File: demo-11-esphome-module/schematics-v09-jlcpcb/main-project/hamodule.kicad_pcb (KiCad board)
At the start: 2 copper layers, 145.4 x 76.2 mm, 64 parts, among them J1 1017505, J2 Conn-ESP-Relays, J3 1017505, J4 Conn-Buttons, J5 Conn_01x02, J6 Conn-Esp-Sensors, J7 Conn-LedIndicators, J8 1017505, J9 Current Jumper, K1 G5Q-1, K2 G5Q-1, K3 G5Q-1, K4 G5Q-1, U1 ULN2003A, U2 LD1117S33TR_SOT223, U3 HCPL3700, U4 HCPL3700, U5 HCPL3700, U6 HCPL3700

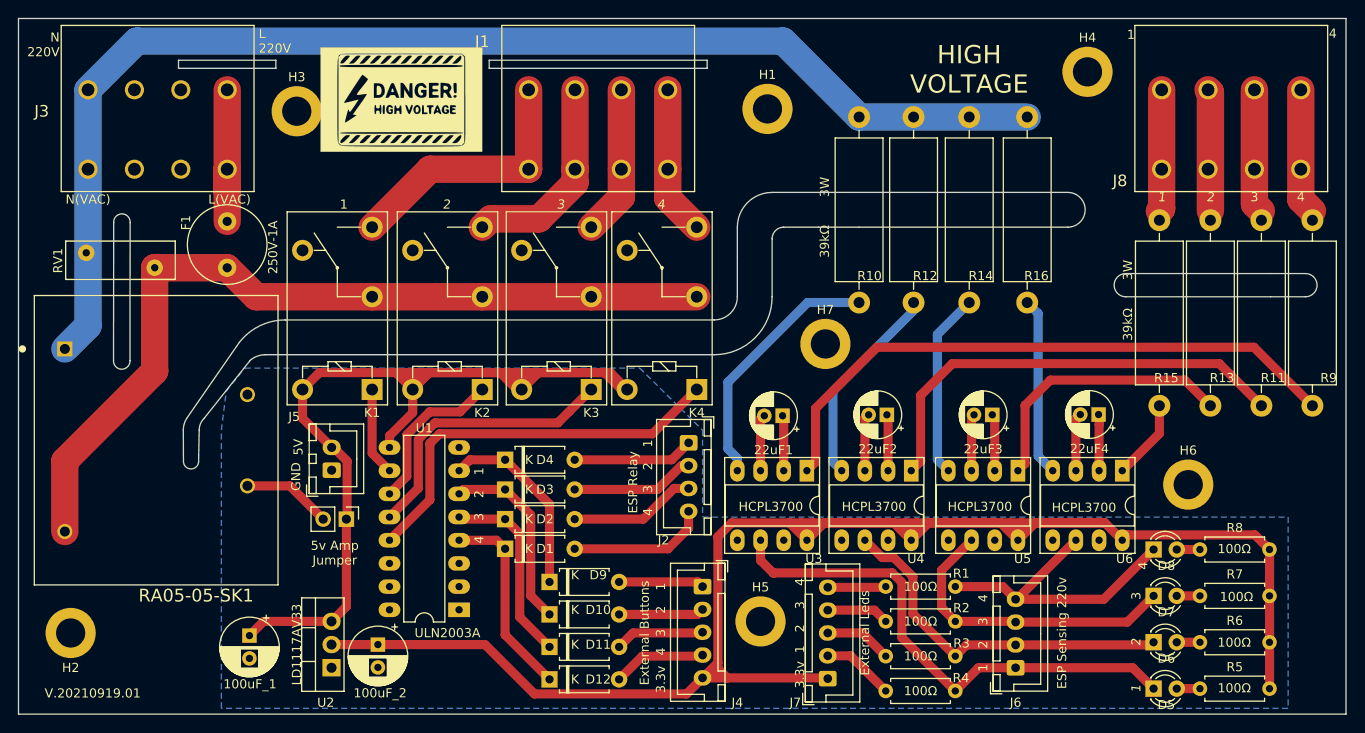
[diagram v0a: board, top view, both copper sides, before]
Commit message: jlcpcb v2: increas connectors pads + fix numbering for sensors in labels
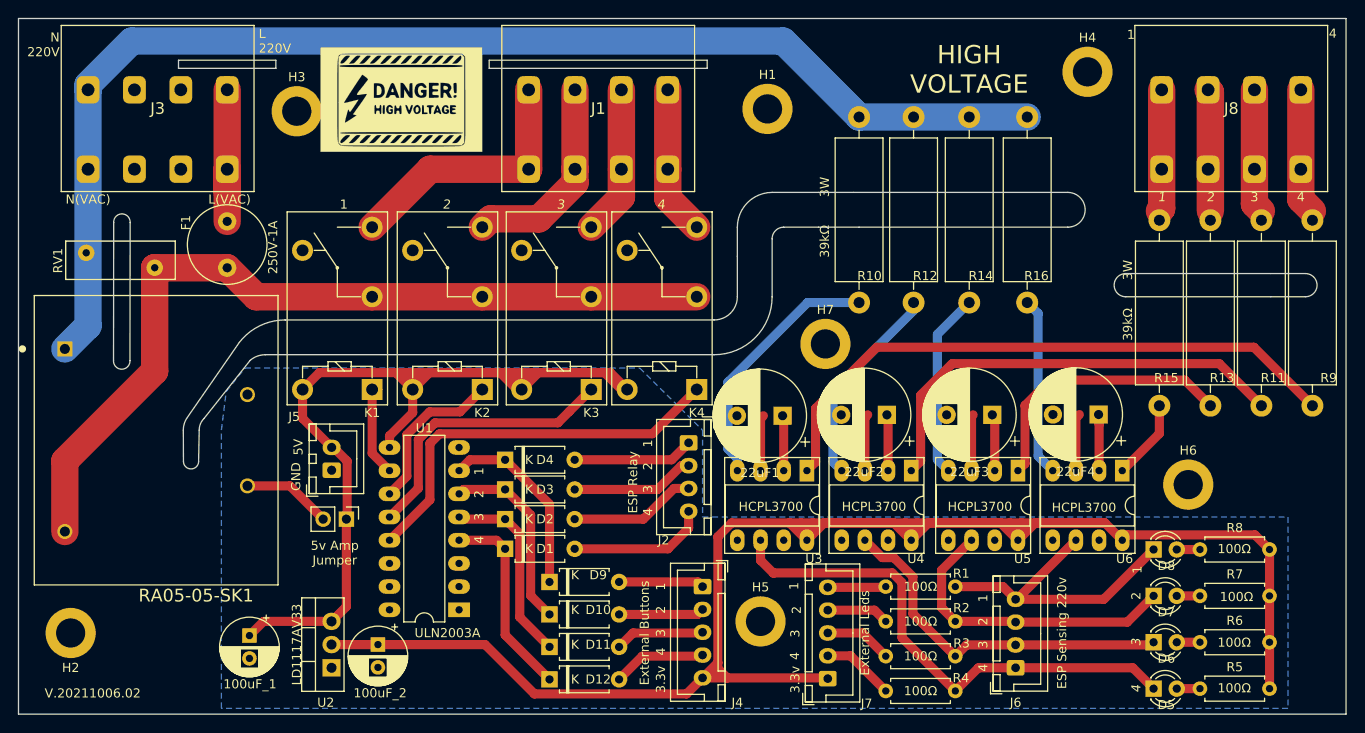
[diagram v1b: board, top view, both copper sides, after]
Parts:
- 22uF1, 22uF2, 22uF3, 22uF4: footprint Capacitor_THT:CP_Radial_D5.0mm_P2.00mm -> Capacitor_THT:CP_Radial_D10.0mm_P5.00mm
- J1, J3, J8: footprint Phoenix_Conn:1017505 -> 1017505_updated_pretty:1017505_pretty
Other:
- board text added: "V.20211006.02"
- board text removed: "V.20210919.01"

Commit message: adding an output fuse
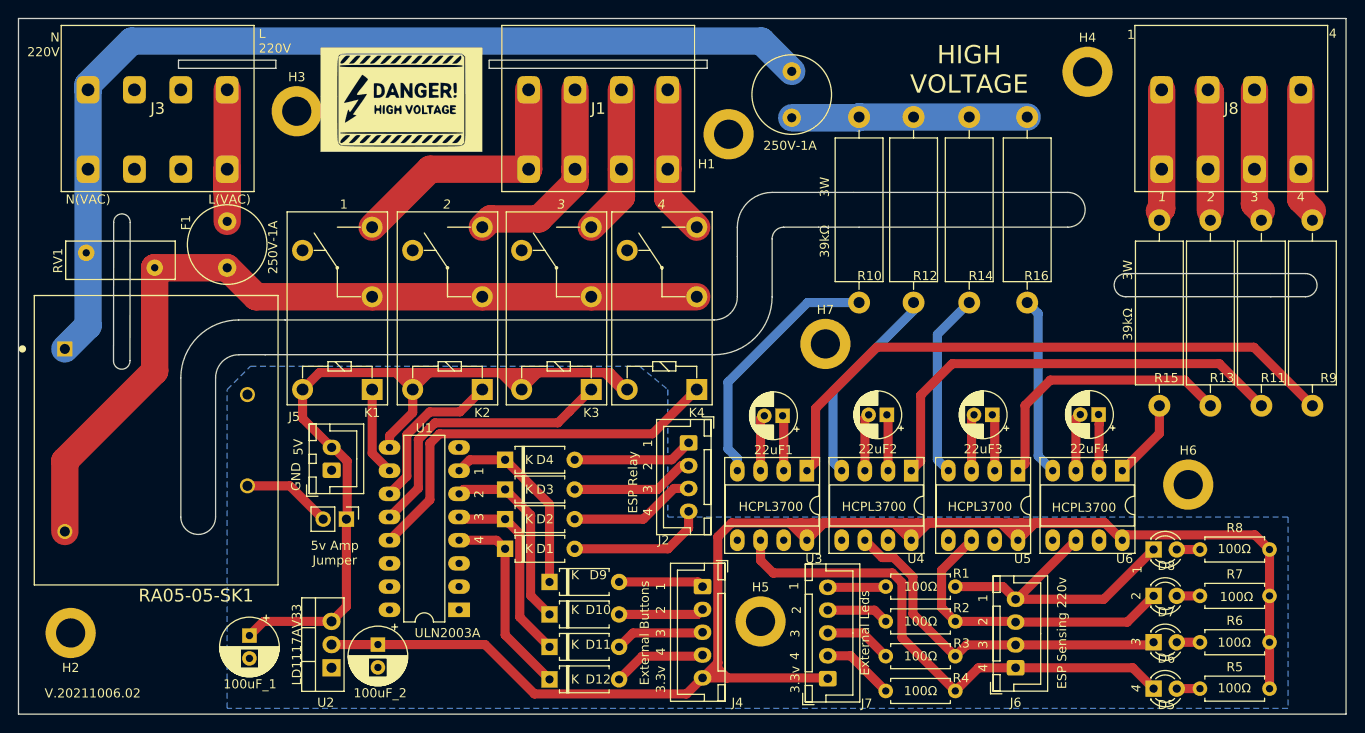
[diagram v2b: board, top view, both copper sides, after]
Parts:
- added 250V-1A: F250V, Fuse:Fuse_Littelfuse_372_D8.50mm, F.Cu at (106.3, 17.2)
- 22uF1, 22uF2, 22uF3, 22uF4: footprint Capacitor_THT:CP_Radial_D10.0mm_P5.00mm -> Capacitor_THT:CP_Radial_D5.0mm_P2.00mm
- F1: value Fuse -> F250V
- moved H1 5.08 mm to (99.4, 24.1)
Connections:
- J3 pad 7: 220VAC(N) -> Net-(F2-Pad1)
- J3 pad 8: 220VAC(N) -> Net-(F2-Pad1)
- RA05-05-SK1 pad 1: 220VAC(N) -> Net-(F2-Pad1)
- RV1 pad 1: 220VAC(N) -> Net-(F2-Pad1)
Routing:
- net 220VAC(N): track 138.3 -> 25.9 mm
- net Net-(F2-Pad1): track 0.00 -> 110.4 mm
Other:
- outline, holes or cut-outs redrawn

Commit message: smd version
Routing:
- net Net-(R14-Pad2): track 20.4 -> 19.4 mm
- net Net-(R10-Pad2): track 28.1 -> 27.2 mm
- net Net-(R12-Pad1): track 22.5 -> 21.7 mm
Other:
- outline, holes or cut-outs redrawn
